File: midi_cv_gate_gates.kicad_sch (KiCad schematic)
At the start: 79 parts, among them U10 74HC595, U11 74HC595, U12 LM358, U13 LM358, U14 LM358, U15 LM358, U16 LM358, U17 LM358, U18 LM358, U19 LM358

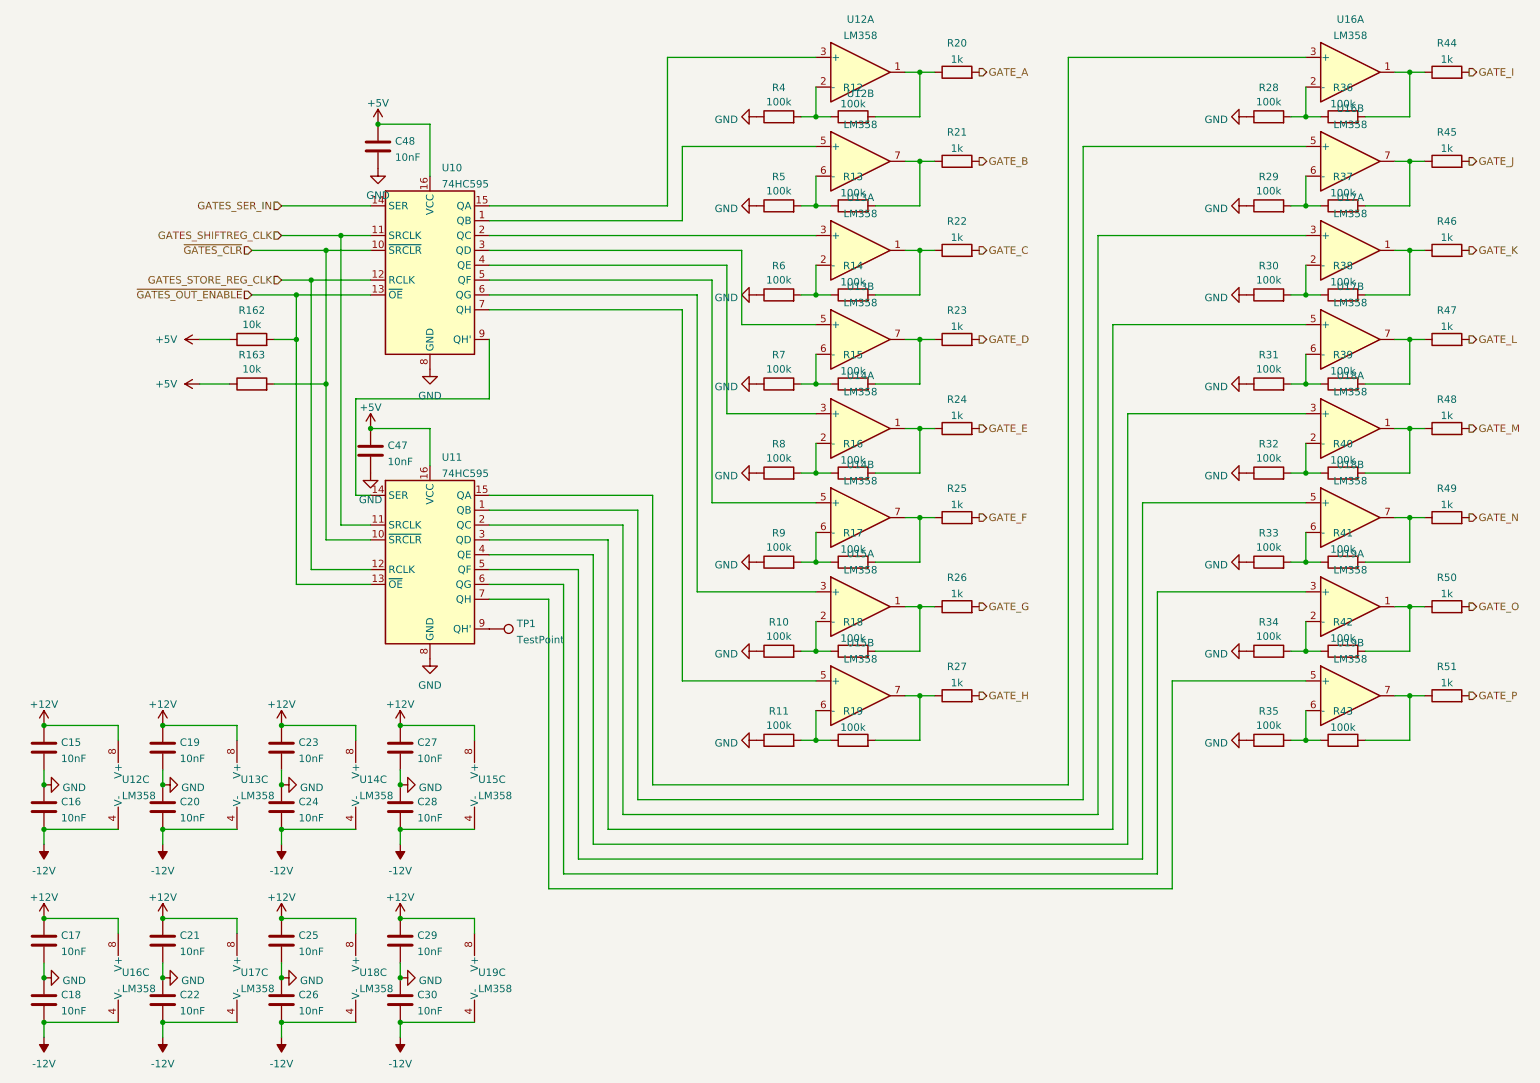
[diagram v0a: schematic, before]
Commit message: Replace soic-14 with dip 14 for DACs, add pulldowns on opamp inputs
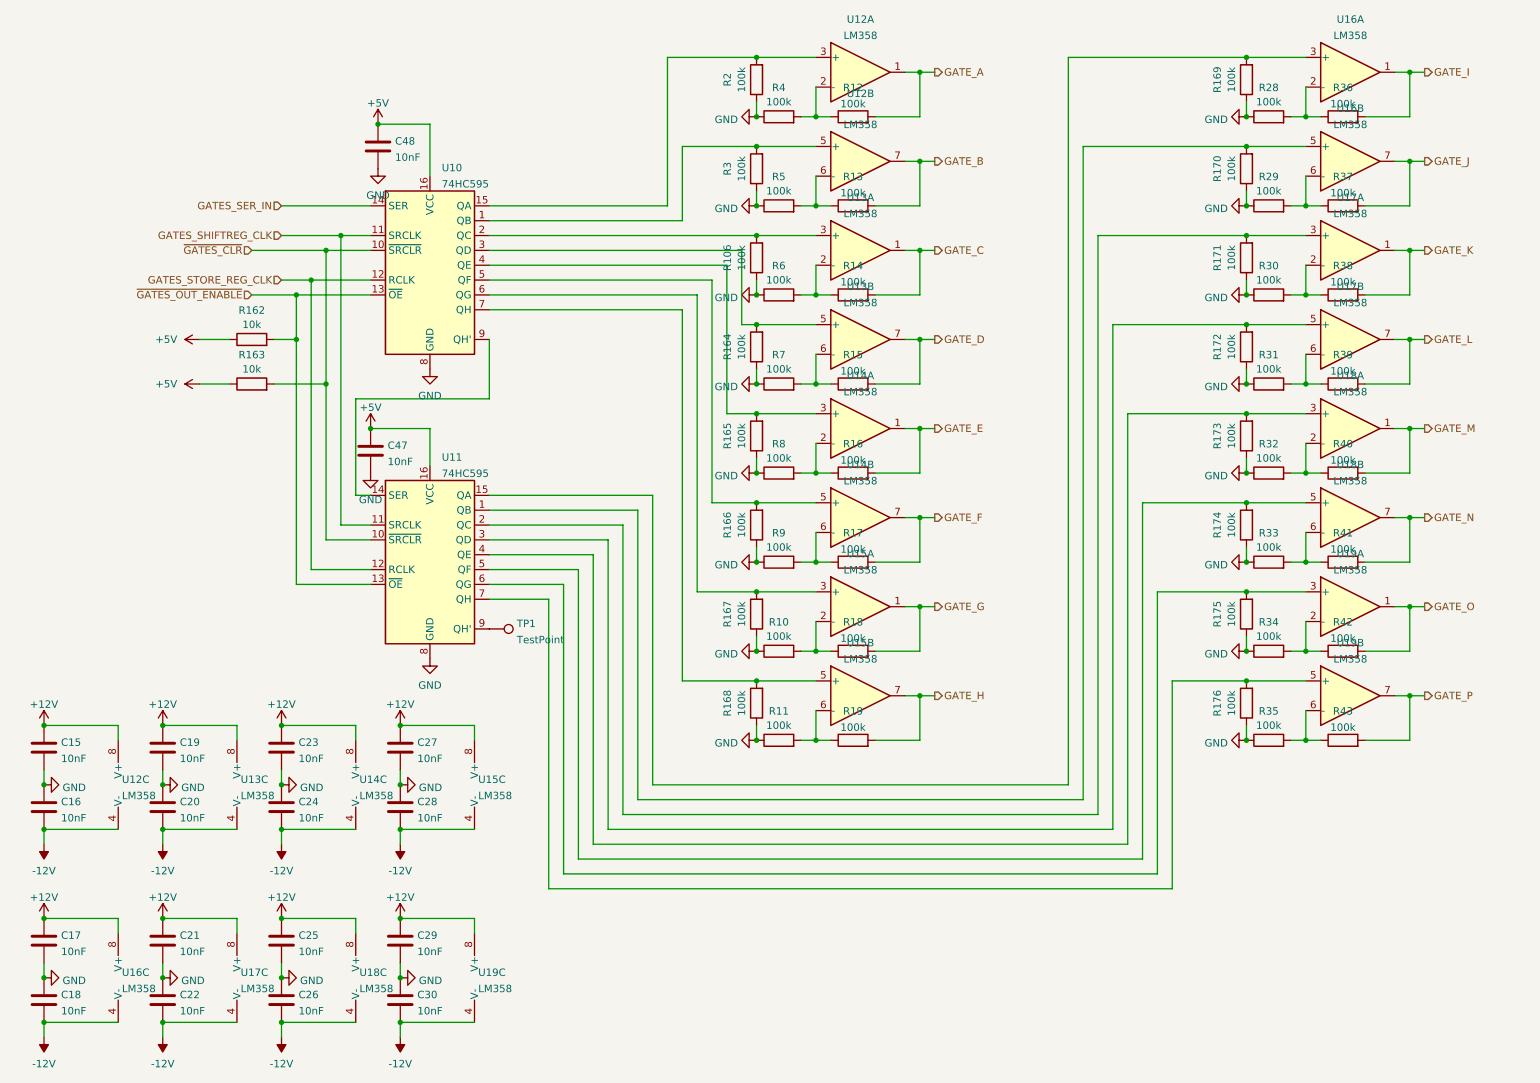
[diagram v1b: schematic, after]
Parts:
- removed R20, R21, R22, R23, R24, R25, R26, R27, R44, R45, R46, R47, R48, R49, R50, R51: 1k, Resistor_SMD:R_1206_3216Metric_Pad1.30x1.75mm_HandSolder, symbol Device:R
- added R106, R164, R165, R166, R167, R168, R169, R170, R171, R172, R173, R174, R175, R176, R2, R3: 100k, Resistor_SMD:R_1206_3216Metric_Pad1.30x1.75mm_HandSolder, symbol Device:R
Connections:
- net GATE_A: now also R12.2, U12.1
- net GATE_B: now also R13.2, U12.7
- net GATE_C: now also R14.2, U13.1
- net GATE_D: now also R15.2, U13.7
- net GATE_E: now also R16.2, U14.1
- net GATE_F: now also R17.2, U14.7
- net GATE_G: now also R18.2, U15.1
- net GATE_H: now also R19.2, U15.7
- net GATE_I: now also R36.2, U16.1
- net GATE_J: now also R37.2, U16.7
- net GATE_K: now also R38.2, U17.1
- net GATE_L: now also R39.2, U17.7
- net GATE_M: now also R40.2, U18.1
- net GATE_N: now also R41.2, U18.7
- net GATE_O: now also R42.2, U19.1
- net GATE_P: now also R43.2, U19.7
- net GND: now also R106.1, R164.1, R165.1, R166.1, R167.1, R168.1, R169.1, R170.1, R171.1, R172.1, R173.1, R174.1, R175.1, R176.1, R2.1, R3.1
- net at U10.15 (QA), U12.3 (+): now also R2.2
- net at U10.4 (QE), U14.3 (+): now also R165.2
- net at U10.1 (QB), U12.5 (+): now also R3.2
- net at U11.4 (QE), U18.3 (+): now also R173.2
- net at U11.6 (QG), U19.3 (+): now also R175.2
- net at U11.1 (QB), U16.5 (+): now also R170.2
- net at U11.15 (QA), U16.3 (+): now also R169.2
- net at U11.2 (QC), U17.3 (+): now also R171.2
- net at U11.3 (QD), U17.5 (+): now also R172.2
- net at U11.5 (QF), U18.5 (+): now also R174.2
- net at U11.7 (QH), U19.5 (+): now also R176.2
- net at U10.2 (QC), U13.3 (+): now also R106.2
- net at U10.6 (QG), U15.3 (+): now also R167.2
- net at U10.3 (QD), U13.5 (+): now also R164.2
- net at U10.7 (QH), U15.5 (+): now also R168.2
- net at U10.5 (QF), U14.5 (+): now also R166.2

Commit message: Routing of main board done
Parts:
- added TP6: QH_1, TestPoint:TestPoint_Pad_D1.0mm, symbol Connector:TestPoint
- TP7: renamed from TP1; value TestPoint -> QH2
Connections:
- net at U10.9 (QH'), U11.14 (SER): now also TP6.1

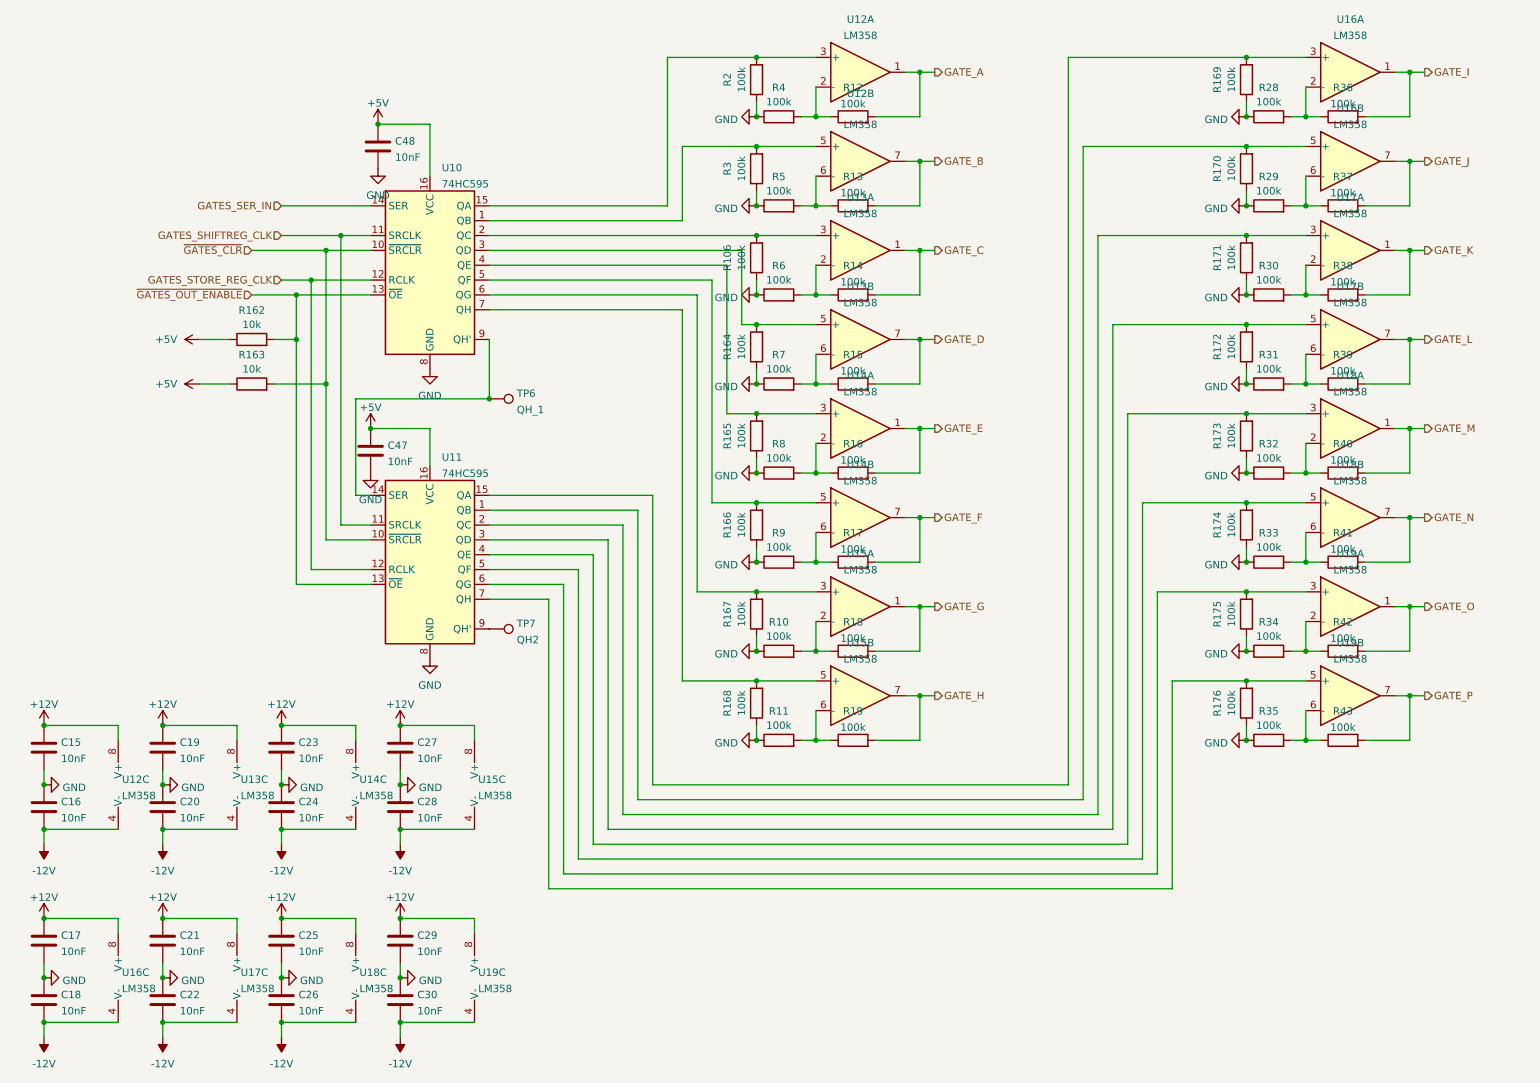
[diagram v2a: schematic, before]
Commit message: Fixed alignment of jacks and LEDs
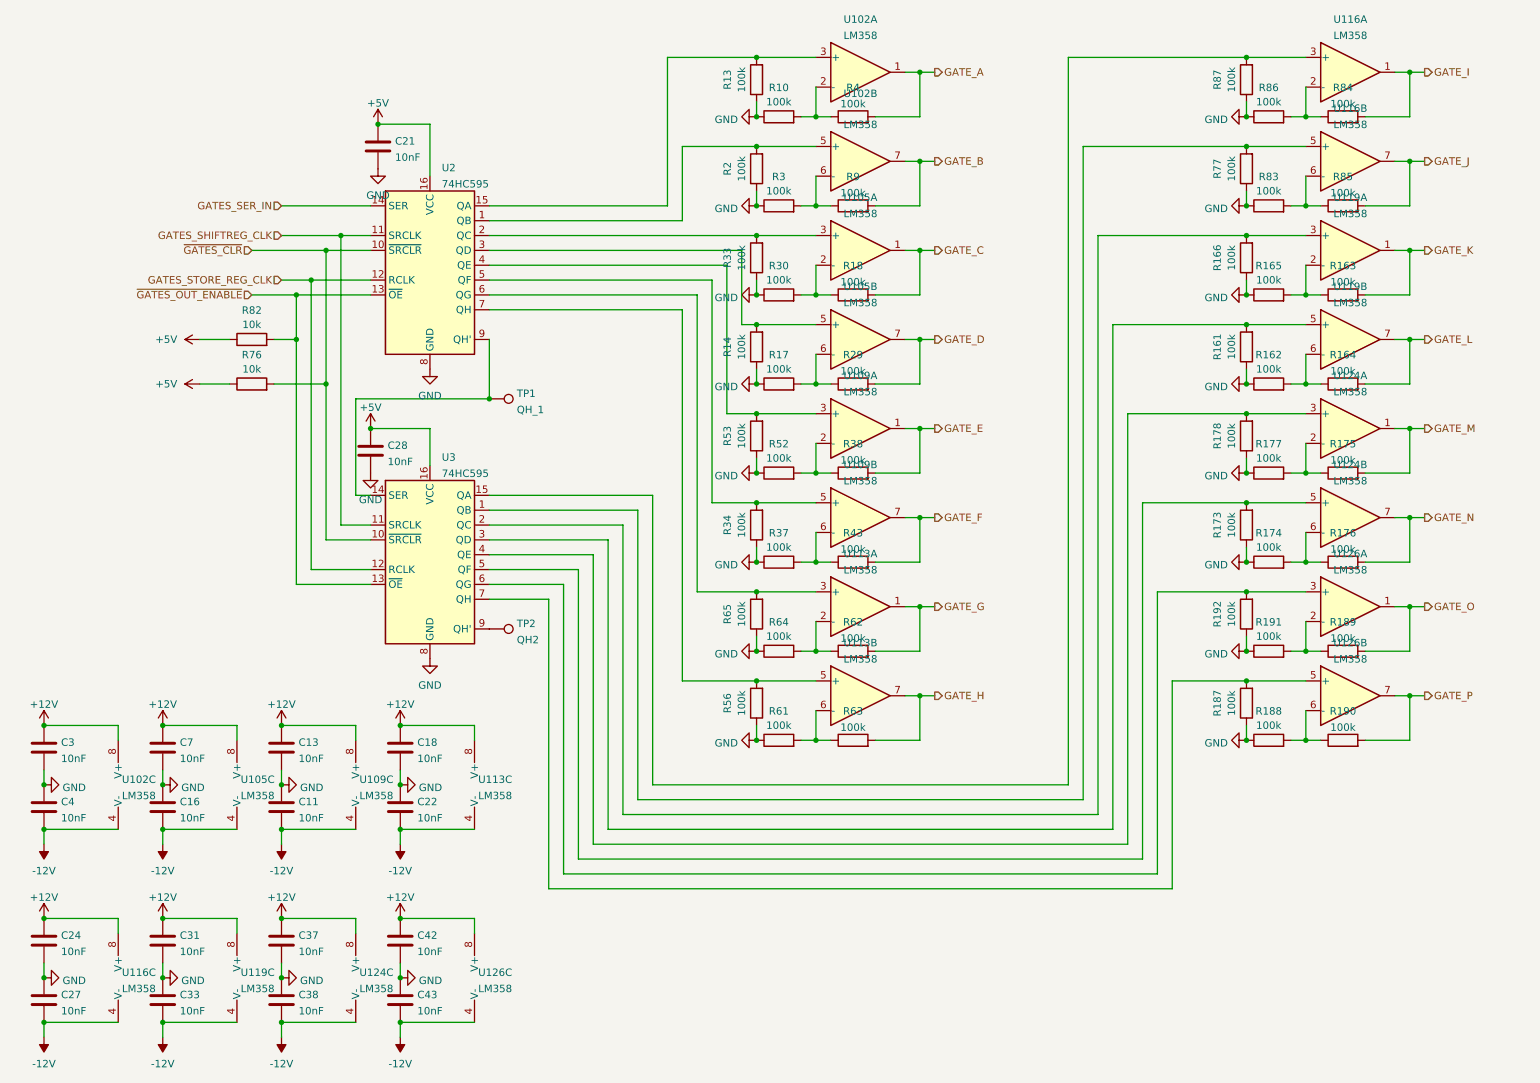
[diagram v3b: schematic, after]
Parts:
- renumbered C24 to C11, C23 to C13, C20 to C16, C27 to C18, C48 to C21, C28 to C22, C17 to C24, C18 to C27, C47 to C28, C15 to C3, C21 to C31, C22 to C33, C25 to C37, C26 to C38, C16 to C4, C29 to C42, C30 to C43, C19 to C7, R4 to R10, R2 to R13, R164 to R14, R172 to R161, R31 to R162, R38 to R163, R39 to R164, R30 to R165, R171 to R166, R7 to R17, R174 to R173, R33 to R174, R40 to R175, R41 to R176, R32 to R177, R173 to R178, R14 to R18, R176 to R187, R35 to R188, R42 to R189, R43 to R190, R34 to R191, R175 to R192, R3 to R2, R15 to R29, R5 to R3, R6 to R30, R106 to R33, R166 to R34, R9 to R37, R16 to R38, R12 to R4, R17 to R43, R8 to R52, R165 to R53, R168 to R56, R11 to R61, R18 to R62, R19 to R63, R10 to R64, R167 to R65, R163 to R76, R170 to R77, R162 to R82, R29 to R83, R36 to R84, R37 to R85, R28 to R86, R169 to R87, R13 to R9, TP6 to TP1, TP7 to TP2, U12 to U102, U13 to U105, U14 to U109, U15 to U113, U16 to U116, U17 to U119, U18 to U124, U19 to U126, U10 to U2, U11 to U3

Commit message: Cleanups and title blocks
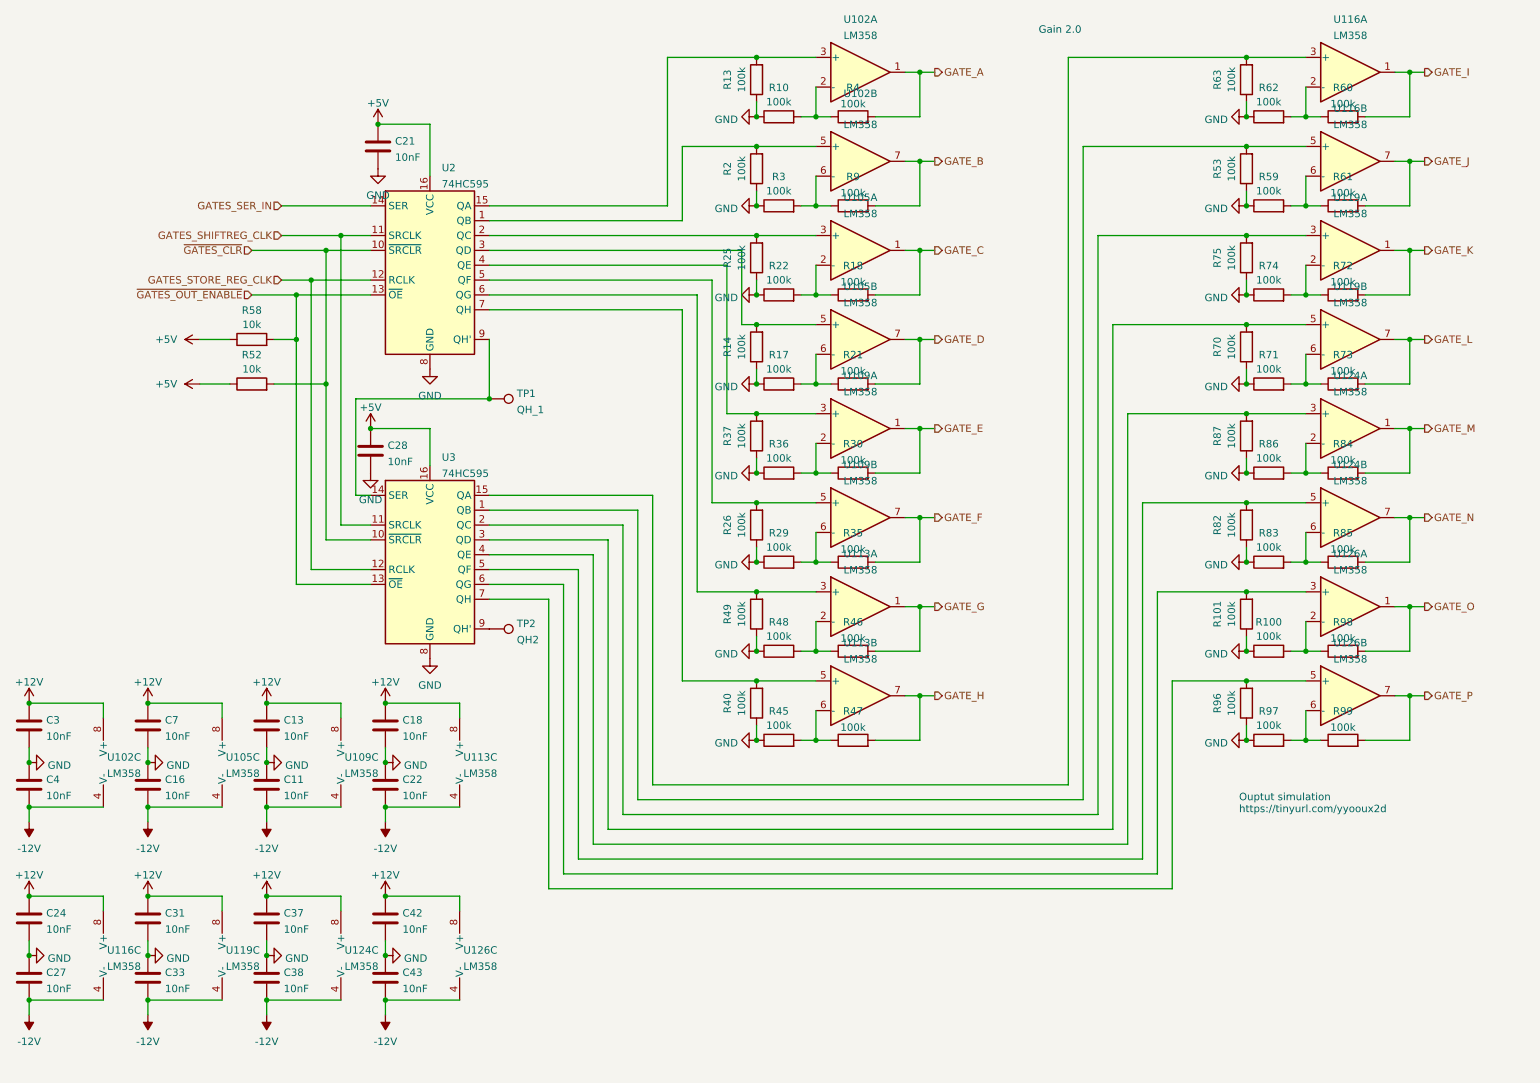
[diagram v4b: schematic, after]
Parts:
- renumbered R191 to R100, R192 to R101, R29 to R21, R30 to R22, R33 to R25, R34 to R26, R37 to R29, R38 to R30, R43 to R35, R52 to R36, R53 to R37, R56 to R40, R61 to R45, R62 to R46, R63 to R47, R64 to R48, R65 to R49, R76 to R52, R77 to R53, R82 to R58, R83 to R59, R84 to R60, R85 to R61, R86 to R62, R87 to R63, R161 to R70, R162 to R71, R163 to R72, R164 to R73, R165 to R74, R166 to R75, R173 to R82, R174 to R83, R175 to R84, R176 to R85, R177 to R86, R178 to R87, R187 to R96, R188 to R97, R189 to R98, R190 to R99
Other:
- note added: "Gain 2.0"
- note added: "Ouptut simulation https://tinyurl.com/yyooux2d"
- company: (none) -> RobotDialogs
- title: (none) -> Eurorack MIDI 16x16 CV Gate
- moved on the sheet: C11, C13, C16, C18, C22, C24, C27, C3, C31, C33, C37, C38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
